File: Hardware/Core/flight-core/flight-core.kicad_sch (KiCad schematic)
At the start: 20 parts, among them J1 Conn_02x02_Remote_ESTOP, J2 Conn_02x04_Counter_Clockwise, J3 Conn_02x05_Counter_Clockwise, J4 Conn_02x05_Counter_Clockwise, J5 Conn_02x05_Counter_Clockwise, J6 Conn_02x05_Counter_Clockwise

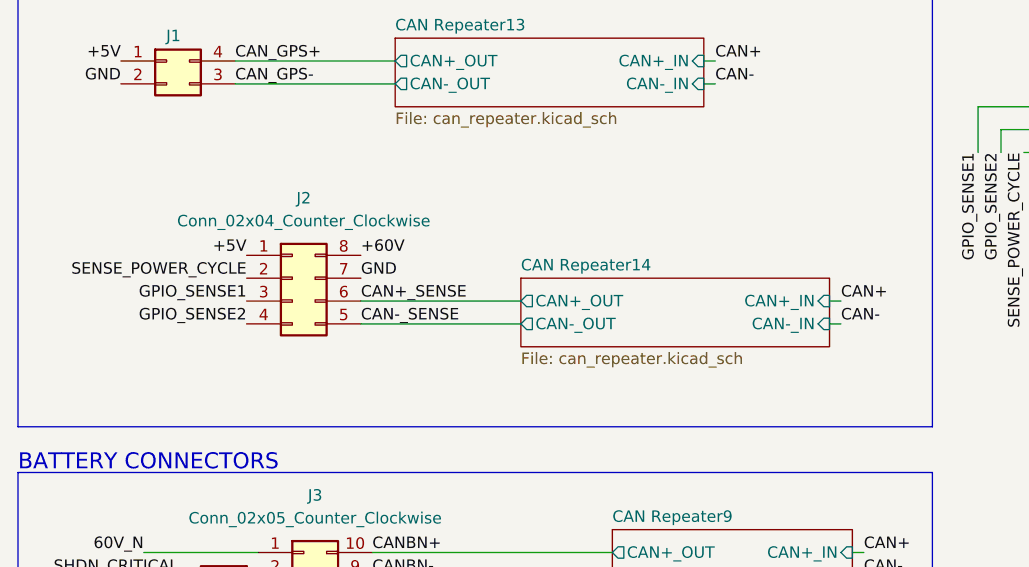
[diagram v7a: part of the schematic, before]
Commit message: fixed new silkscreen and courtyard drc errors, flipped middle connector
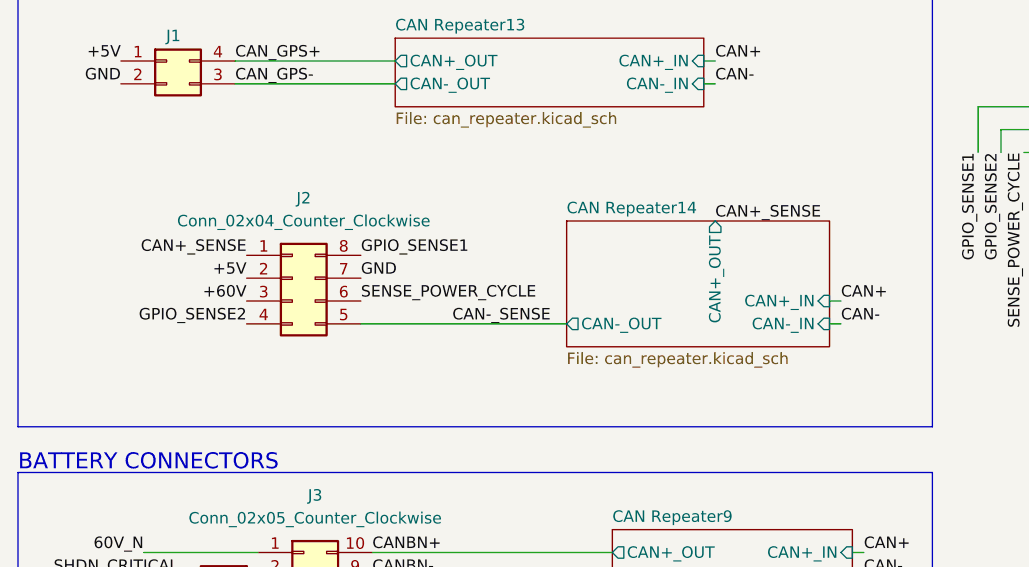
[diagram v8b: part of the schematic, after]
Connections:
- net +5V: now also J2.2 (Pin_2); no longer J2.1 (Pin_1)
- net +BATT: now also J2.3 (Pin_3); no longer J2.8 (Pin_8)
- net CAN+_SENSE: now also J2.1 (Pin_1); no longer J2.6 (Pin_6)
- net GPIO_SENSE1: now also J2.8 (Pin_8); no longer J2.3 (Pin_3)
- net SENSE_POWER_CYCLE: now also J2.6 (Pin_6); no longer J2.2 (Pin_2)
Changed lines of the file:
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@@
 	(wire
 		(pts
+			(xy 57.15 62.23) (xy 80.01 62.23)
+		)
+		(stroke
+			(width 0)
+			(type default)
+		)
+	)
+	(wire
+		(pts
 			(xy 170.18 85.09) (xy 241.3 85.09)
 		)
@@
 	(wire
 		(pts
-			(xy 57.15 62.23) (xy 74.93 62.23)
-		)
-		(stroke
-			(width 0)
-			(type default)
-		)
-	)
-	(wire
-		(pts
 			(xy 177.8 41.91) (xy 185.42 41.91)
 		)
@@
 	(wire
 		(pts
-			(xy 57.15 59.69) (xy 74.93 59.69)
-		)
-		(stroke
-			(width 0)
-			(type default)
-		)
-	)
-	(wire
-		(pts
 			(xy 232.41 57.15) (xy 232.41 43.18)
 		)
@@
 		)
 	)
+	(label "CAN+_SENSE"
+		(at 96.52 50.8 0)
+		(effects
+			(font
+				(size 1.27 1.27)
+			)
+			(justify left bottom)
+		)
+	)
 	(label "CANBN-"
 		(at 58.42 90.17 0)
@@
 	)
 	(label "CAN+_SENSE"
-		(at 57.15 59.69 0)
+		(at 44.45 54.61 180)
 		(effects
 			(font
 				(size 1.27 1.27)
 			)
-			(justify left bottom)
+			(justify right bottom)
 		)
 	)
@@
 	)
 	(label "CAN-_SENSE"
-		(at 57.15 62.23 0)
+		(at 67.31 62.23 0)
 		(effects
 			(font
@@
 	)
 	(label "+5V"
-		(at 44.45 54.61 180)
+		(at 44.45 57.15 180)
 		(effects
 			(font
@@
 	)
 	(label "SENSE_POWER_CYCLE"
-		(at 44.45 57.15 180)
+		(at 57.15 59.69 0)
 		(effects
 			(font
 				(size 1.27 1.27)
 			)
-			(justify right bottom)
+			(justify left bottom)
 		)
 	)
@@
 	)
 	(label "+60V"
-		(at 57.15 54.61 0)
+		(at 44.45 59.69 180)
 		(effects
 			(font
 				(size 1.27 1.27)
 			)
-			(justify left bottom)
+			(justify right bottom)
 		)
 	)
@@
 	)
 	(label "GPIO_SENSE1"
-		(at 44.45 59.69 180)
+		(at 57.15 54.61 0)
 		(effects
 			(font
 				(size 1.27 1.27)
 			)
-			(justify right bottom)
+			(justify left bottom)
 		)
 	)
@@
 	)
 	(sheet
-		(at 74.93 57.15)
-		(size 34.29 7.62)
+		(at 80.01 50.8)
+		(size 29.21 13.97)
 		(exclude_from_sim no)
 		(in_bom yes)
@@
 		)
 		(property "Sheetname" "CAN Repeater14"
-			(at 74.93 56.4384 0)
+			(at 80.01 50.0884 0)
 			(effects
 				(font
@@
 		)
 		(property "Sheetfile" "can_repeater.kicad_sch"
-			(at 74.93 65.3546 0)
+			(at 80.01 65.3546 0)
 			(effects
 				(font
@@
 		)
 		(pin "CAN-_OUT" output
-			(at 74.93 62.23 180)
+			(at 80.01 62.23 180)
 			(effects
 				(font
@@
 		)
 		(pin "CAN+_OUT" output
-			(at 74.93 59.69 180)
+			(at 96.52 50.8 90)
 			(effects
 				(font
 					(size 1.27 1.27)
 				)
-				(justify left)
+				(justify right)
 			)
 		)
